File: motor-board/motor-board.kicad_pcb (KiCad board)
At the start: 2 copper layers, 52.6 x 40.9 mm, 12 parts, among them J1 Motor Driver IN, J2 Motor Driver OUT, J3 Regulator, J4 Ribbon Connector, J5 Battery, J6 Cape Power, J7 Right Motor JST, J8 Left Motor JST

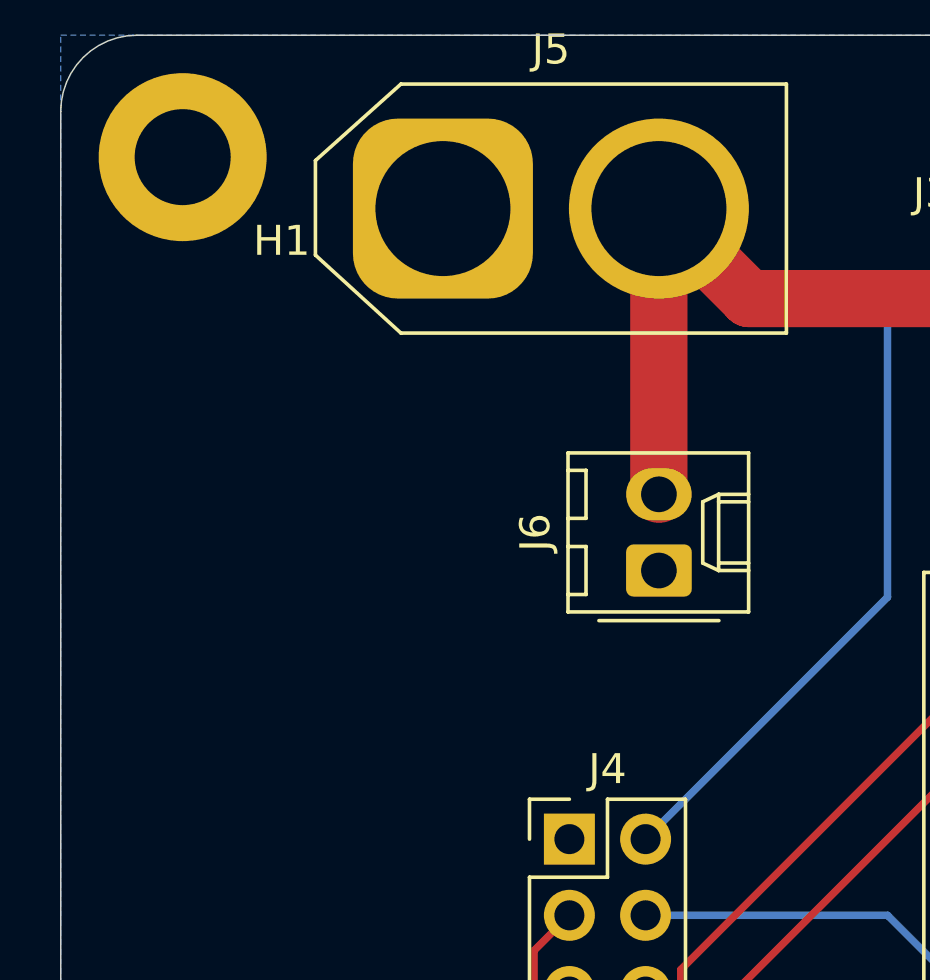
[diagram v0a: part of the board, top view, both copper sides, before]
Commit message: Updated b2b power connector to 4-pin
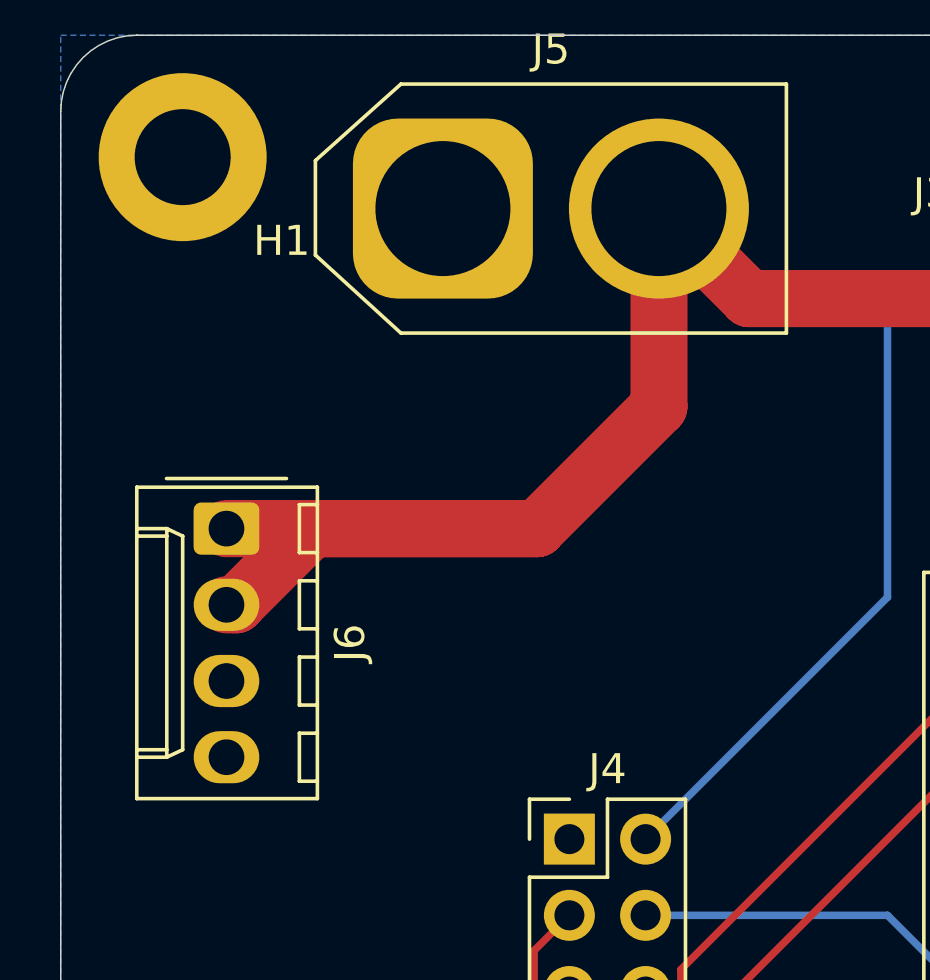
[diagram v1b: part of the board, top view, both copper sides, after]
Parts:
- J6: value Cape Power -> Conn_01x04; footprint Connector_Molex:Molex_KK-254_AE-6410-02A_1x02_P2.54mm_Vertical -> Connector_Molex:Molex_KK-254_AE-6410-04A_1x04_P2.54mm_Vertical
- moved J6 14.5 mm to (99.3, 72.1), turned to 270 degrees
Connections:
- J6 pad 1: GNDD -> +BATT
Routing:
- net +BATT: track 27.7 -> 52.3 mm

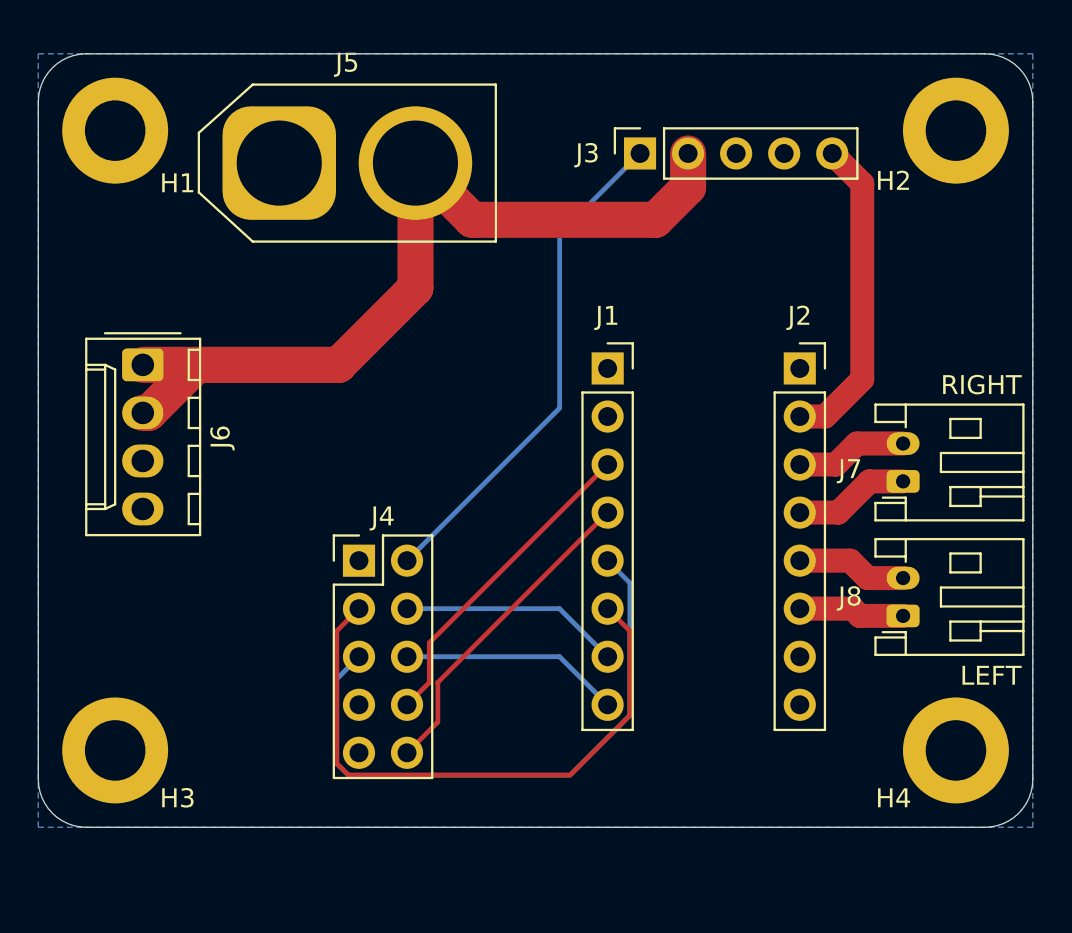
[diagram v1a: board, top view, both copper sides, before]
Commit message: Fixed b2b power header names, improved motor board layout
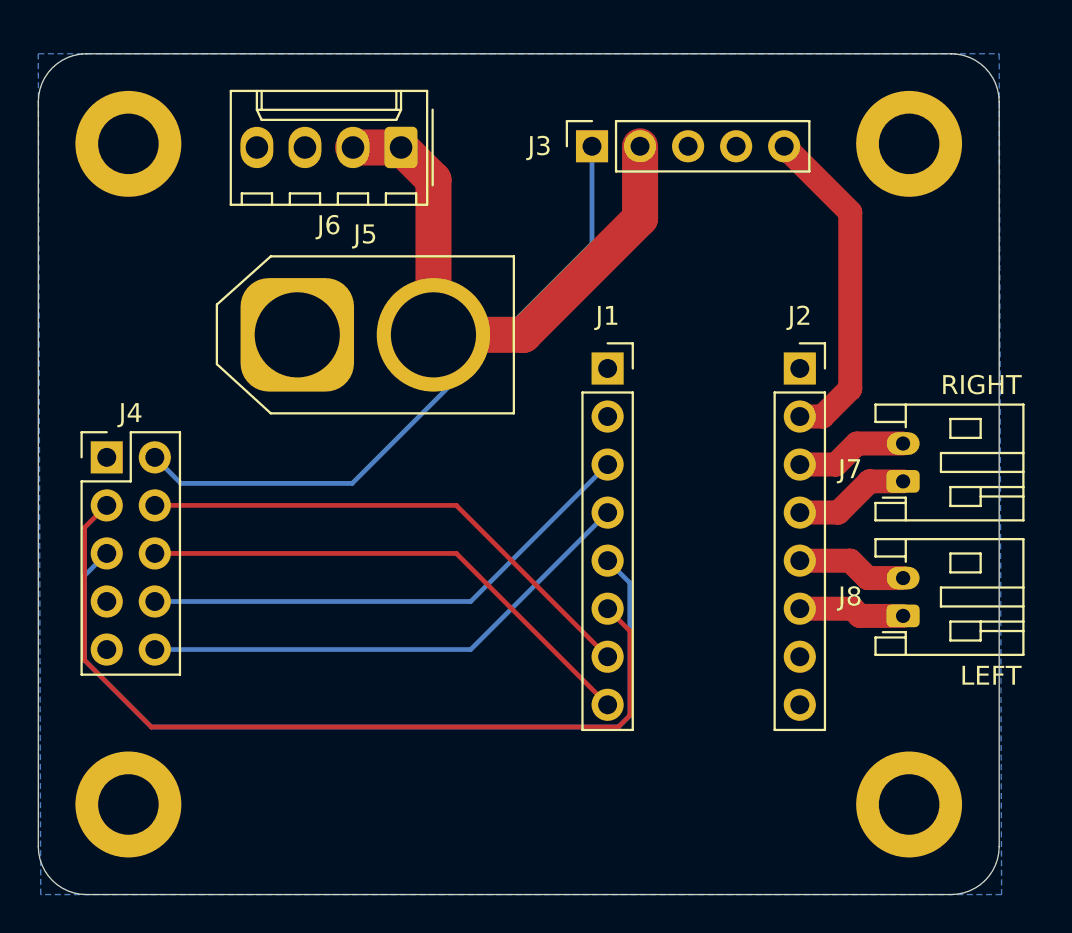
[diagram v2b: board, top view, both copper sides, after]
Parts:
- moved J6 17.8 mm to (112.9, 60.6), turned to 180 degrees
- moved J4 14.4 mm to (97.3, 77.0)
- moved J5 9.13 mm to (107.4, 70.5)
- moved H4 3.78 mm to (139.8, 95.3)
- moved H3 2.94 mm to (98.5, 95.3)
- moved H2 2.57 mm to (139.8, 60.4)
- moved J3 2.57 mm to (123.0, 60.5)
- moved H1 0.99 mm to (98.5, 60.4)
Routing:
- net +BATT: track 52.3 -> 30.4 mm
- net MOTOR_nSLEEP: track 11.7 -> 27.3 mm
- net MOTOR_nFAULT: track 11.7 -> 27.3 mm
- net MOTOR_PWM_LEFT_B: track 31.9 -> 45.3 mm
- net MOTOR_PWM_LEFT_A: track 31.9 -> 45.3 mm
- net MOTOR_PWM_RIGHT_B: track 17.1 -> 26.9 mm
- net MOTOR_PWM_RIGHT_A: track 17.1 -> 26.9 mm
- net MOTOR_PWR_EN: track 26.6 -> 34.1 mm
- net +5V: track 16.7 -> 17.5 mm
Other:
- board size 52.6 x 40.9 mm -> 50.8 x 44.5 mm

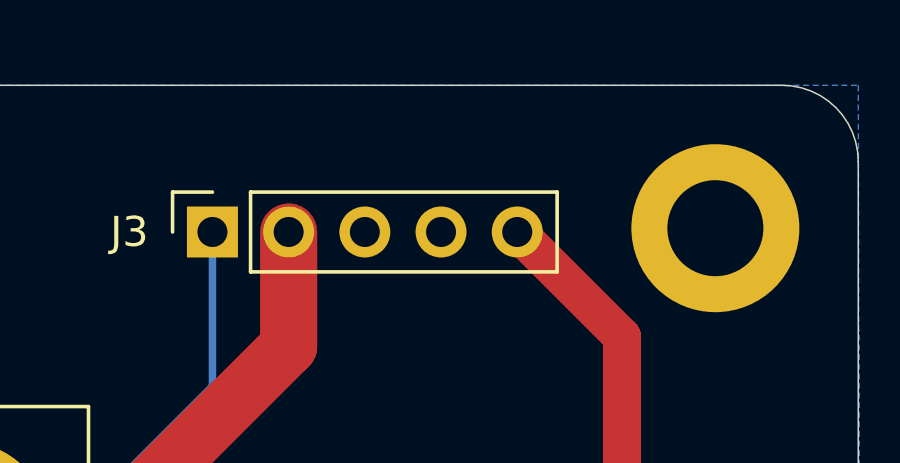
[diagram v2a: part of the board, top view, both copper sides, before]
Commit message: Added power LED to motor board
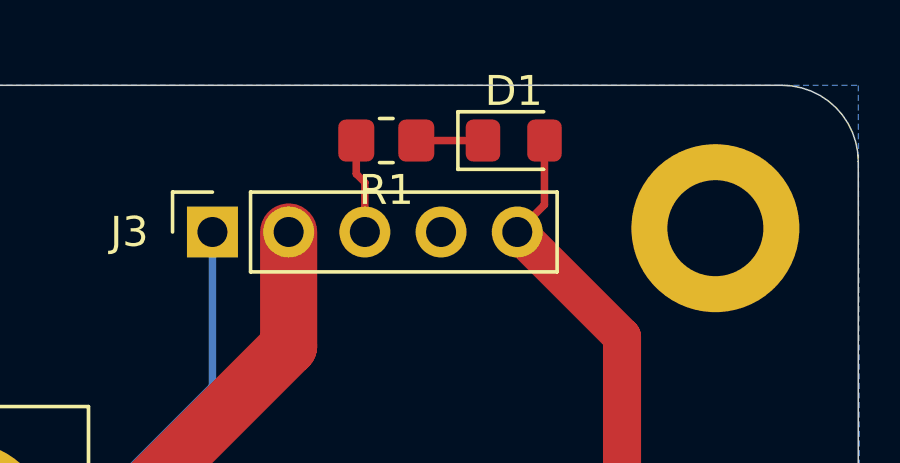
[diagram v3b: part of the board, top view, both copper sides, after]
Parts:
- added D1: POWER_LED, LED_SMD:LED_0805_2012Metric_Pad1.15x1.40mm_HandSolder, F.Cu at (133.0, 57.5)
- added R1: R, Resistor_SMD:R_0805_2012Metric_Pad1.20x1.40mm_HandSolder, F.Cu at (128.8, 57.5)
- J6: value Conn_01x04 -> BoardToBoardPower
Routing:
- net +5V: track 17.5 -> 21.0 mm
- net GNDD: track 0.00 -> 3.17 mm
- net Net-(D1-Pad1): track 0.00 -> 2.22 mm
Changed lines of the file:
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@@
     (thickness 1.6)
     (drawings 21)
-    (tracks 48)
+    (tracks 54)
     (zones 0)
-    (modules 12)
-    (nets 20)
+    (modules 14)
+    (nets 21)
   )
   (page A4)
@@
   (net 18 "Net-(J4-Pad7)")
   (net 19 "Net-(J4-Pad9)")
+  (net 20 "Net-(D1-Pad1)")
   (net_class Default "This is the default net class."
     (clearance 0.2)
@@
     (add_net MOTOR_nFAULT)
     (add_net MOTOR_nSLEEP)
+    (add_net "Net-(D1-Pad1)")
     (add_net "Net-(J1-Pad2)")
     (add_net "Net-(J2-Pad7)")
@@
       (effects (font (size 1 1) (thickness 0.15)))
     )
-    (fp_text value Conn_01x04 (at 3.81 4.08) (layer F.Fab)
+    (fp_text value BoardToBoardPower (at 3.81 4.08) (layer F.Fab)
       (effects (font (size 1 1) (thickness 0.15)))
     )
@@
     )
   )
+  (module LED_SMD:LED_0805_2012Metric_Pad1.15x1.40mm_HandSolder (layer F.Cu)
+    (at 133.0415 57.4675)
+    (descr "LED SMD 0805 (2012 Metric), square (rectangular) end terminal, IPC_7351 nominal, (Body size source: https://docs.google.com/spreadsheets/d/1BsfQQcO9C6DZCsRaXUlFlo91Tg2WpOkGARC1WS5S8t0/edit?usp=sharing), generated with kicad-footprint-generator")
+    (tags "LED handsolder")
+    (attr smd)
+    (fp_text reference D1 (at 0 -1.65) (layer F.SilkS)
+      (effects (font (size 1 1) (thickness 0.15)))
+    )
+    (fp_text value POWER_LED (at 0 1.65) (layer F.Fab)
+      (effects (font (size 1 1) (thickness 0.15)))
+    )
+    (fp_line (start 1.85 0.95) (end -1.85 0.95) (layer F.CrtYd) (width 0.05))
+    (fp_line (start 1.85 -0.95) (end 1.85 0.95) (layer F.CrtYd) (width 0.05))
+    (fp_line (start -1.85 -0.95) (end 1.85 -0.95) (layer F.CrtYd) (width 0.05))
+    (fp_line (start -1.85 0.95) (end -1.85 -0.95) (layer F.CrtYd) (width 0.05))
+    (fp_line (start -1.86 0.96) (end 1 0.96) (layer F.SilkS) (width 0.12))
+    (fp_line (start -1.86 -0.96) (end -1.86 0.96) (layer F.SilkS) (width 0.12))
+    (fp_line (start 1 -0.96) (end -1.86 -0.96) (layer F.SilkS) (width 0.12))
+    (fp_line (start 1 0.6) (end 1 -0.6) (layer F.Fab) (width 0.1))
+    (fp_line (start -1 0.6) (end 1 0.6) (layer F.Fab) (width 0.1))
+    (fp_line (start -1 -0.3) (end -1 0.6) (layer F.Fab) (width 0.1))
+    (fp_line (start -0.7 -0.6) (end -1 -0.3) (layer F.Fab) (width 0.1))
+    (fp_line (start 1 -0.6) (end -0.7 -0.6) (layer F.Fab) (width 0.1))
+    (fp_text user %R (at 0 0) (layer F.Fab)
+      (effects (font (size 0.5 0.5) (thickness 0.08)))
+    )
+    (pad 1 smd roundrect (at -1.025 0) (size 1.15 1.4) (layers F.Cu F.Paste F.Mask) (roundrect_rratio 0.217391)
+      (net 20 "Net-(D1-Pad1)"))
+    (pad 2 smd roundrect (at 1.025 0) (size 1.15 1.4) (layers F.Cu F.Paste F.Mask) (roundrect_rratio 0.217391)
+      (net 9 +5V))
+    (model ${KISYS3DMOD}/LED_SMD.3dshapes/LED_0805_2012Metric.wrl
+      (at (xyz 0 0 0))
+      (scale (xyz 1 1 1))
+      (rotate (xyz 0 0 0))
+    )
+  )
+  (module Resistor_SMD:R_0805_2012Metric_Pad1.20x1.40mm_HandSolder (layer F.Cu)
+    (at 128.794 57.4675 180)
+    (descr "Resistor SMD 0805 (2012 Metric), square (rectangular) end terminal, IPC_7351 nominal with elongated pad for handsoldering. (Body size source: IPC-SM-782 page 72, https://www.pcb-3d.com/wordpress/wp-content/uploads/ipc-sm-782a_amendment_1_and_2.pdf), generated with kicad-footprint-generator")
+    (tags "resistor handsolder")
+    (attr smd)
+    (fp_text reference R1 (at 0 -1.65) (layer F.SilkS)
+      (effects (font (size 1 1) (thickness 0.15)))
+    )
+    (fp_text value R (at 0 1.65) (layer F.Fab)
+      (effects (font (size 1 1) (thickness 0.15)))
+    )
+    (fp_line (start 1.85 0.95) (end -1.85 0.95) (layer F.CrtYd) (width 0.05))
+    (fp_line (start 1.85 -0.95) (end 1.85 0.95) (layer F.CrtYd) (width 0.05))
+    (fp_line (start -1.85 -0.95) (end 1.85 -0.95) (layer F.CrtYd) (width 0.05))
+    (fp_line (start -1.85 0.95) (end -1.85 -0.95) (layer F.CrtYd) (width 0.05))
+    (fp_line (start -0.227064 0.735) (end 0.227064 0.735) (layer F.SilkS) (width 0.12))
+    (fp_line (start -0.227064 -0.735) (end 0.227064 -0.735) (layer F.SilkS) (width 0.12))
+    (fp_line (start 1 0.625) (end -1 0.625) (layer F.Fab) (width 0.1))
+    (fp_line (start 1 -0.625) (end 1 0.625) (layer F.Fab) (width 0.1))
+    (fp_line (start -1 -0.625) (end 1 -0.625) (layer F.Fab) (width 0.1))
+    (fp_line (start -1 0.625) (end -1 -0.625) (layer F.Fab) (width 0.1))
+    (fp_text user %R (at 0 0) (layer F.Fab)
+      (effects (font (size 0.5 0.5) (thickness 0.08)))
+    )
+    (pad 1 smd roundrect (at -1 0 180) (size 1.2 1.4) (layers F.Cu F.Paste F.Mask) (roundrect_rratio 0.208333)
+      (net 20 "Net-(D1-Pad1)"))
+    (pad 2 smd roundrect (at 1 0 180) (size 1.2 1.4) (layers F.Cu F.Paste F.Mask) (roundrect_rratio 0.208333)
+      (net 1 GNDD))
+    (model ${KISYS3DMOD}/Resistor_SMD.3dshapes/R_0805_2012Metric.wrl
+      (at (xyz 0 0 0))
+      (scale (xyz 1 1 1))
+      (rotate (xyz 0 0 0))
+    )
+  )
   (dimension 44.45 (width 0.15) (layer Dwgs.User)
     (gr_text "1.7500 in" (at 81.6945 77.851 270) (layer Dwgs.User)
@@
     (arrow2b (pts (xy 123.825 93.726) (xy 124.951504 93.139579)))
   )
+  (segment (start 128.0795 60.5155) (end 128.0795 58.8645) (width 0.25) (layer F.Cu) (net 1))
+  (segment (start 127.794 58.579) (end 127.794 57.4675) (width 0.25) (layer F.Cu) (net 1))
+  (segment (start 128.0795 58.8645) (end 127.794 58.579) (width 0.25) (layer F.Cu) (net 1))
   (segment (start 116.586 84.582) (end 123.825 77.343) (width 0.25) (layer B.Cu) (net 3))
   (segment (start 99.8855 84.582) (end 116.586 84.582) (width 0.25) (layer B.Cu) (net 3))
@@
   (segment (start 136.652 64.008) (end 133.1595 60.5155) (width 1.27) (layer F.Cu) (net 9))
   (segment (start 136.652 73.338081) (end 136.652 64.008) (width 1.27) (layer F.Cu) (net 9))
+  (segment (start 134.0665 59.6085) (end 134.0665 57.4675) (width 0.25) (layer F.Cu) (net 9))
+  (segment (start 133.1595 60.5155) (end 134.0665 59.6085) (width 0.25) (layer F.Cu) (net 9))
   (segment (start 133.985 77.343) (end 135.89 77.343) (width 1.27) (layer F.Cu) (net 10))
   (segment (start 137.001 76.232) (end 139.446 76.232) (width 1.27) (layer F.Cu) (net 10))
@@
   (segment (start 125.5395 64.3255) (end 125.5395 60.5155) (width 1.905) (layer F.Cu) (net 15))
   (segment (start 119.38 70.485) (end 125.5395 64.3255) (width 1.905) (layer F.Cu) (net 15))
+  (segment (start 129.794 57.4675) (end 132.0165 57.4675) (width 0.25) (layer F.Cu) (net 20))
   (zone (net 1) (net_name GNDD) (layer B.Cu) (hatch edge 0.508)
     (connect_pads (clearance 0.508))
